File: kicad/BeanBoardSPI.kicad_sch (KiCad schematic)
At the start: 38 parts, among them J1 Power, J10 SPI6, J11 GPO, J12 GPO, J13 GPI, J14 GPI, J15 Power, J2 Address, J3 Data / Control, J4 SPI0 (RA8875), J5 SPI1, J6 SPI2, J7 SPI3, J8 SPI4, J9 SPI5, U1 74LS42, U10 74LS138, U2 74LS299, U3 74LS161, U4 74LS373, U5 74LS00, U6 74LS00, U7 74LS04, U8 74LS02, U9 74LS74

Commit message: Update BeanBoardSPI.kicad_sch
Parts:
- J1: footprint Connector_PinHeader_2.54mm:PinHeader_1x03_P2.54mm_Vertical -> AltFootprints:PinHeader_1x03_P2.54mm_Vertical
- J12, J13: footprint Connector_PinHeader_2.54mm:PinHeader_1x10_P2.54mm_Vertical -> AltFootprints:PinHeader_1x10_P2.54mm_Vertical
- J2, J3: footprint Connector_PinHeader_2.54mm:PinHeader_1x16_P2.54mm_Vertical -> AltFootprints:PinHeader_1x16_P2.54mm_Vertical
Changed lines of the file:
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@@
       (effects (font (size 1.27 1.27)))
     )
-    (property "Footprint" "Connector_PinHeader_2.54mm:PinHeader_1x03_P2.54mm_Vertical" (at 73.66 13.97 0)
+    (property "Footprint" "AltFootprints:PinHeader_1x03_P2.54mm_Vertical" (at 73.66 13.97 0)
       (effects (font (size 1.27 1.27)) hide)
     )
@@
       (effects (font (size 1.27 1.27)))
     )
-    (property "Footprint" "Connector_PinHeader_2.54mm:PinHeader_1x16_P2.54mm_Vertical" (at 55.88 31.75 0)
+    (property "Footprint" "AltFootprints:PinHeader_1x16_P2.54mm_Vertical" (at 55.88 31.75 0)
       (effects (font (size 1.27 1.27)) hide)
     )
@@
       (effects (font (size 1.27 1.27)))
     )
-    (property "Footprint" "Connector_PinHeader_2.54mm:PinHeader_1x10_P2.54mm_Vertical" (at 73.66 38.1 0)
+    (property "Footprint" "AltFootprints:PinHeader_1x10_P2.54mm_Vertical" (at 73.66 38.1 0)
       (effects (font (size 1.27 1.27)) hide)
     )
@@
       (effects (font (size 1.27 1.27)))
     )
-    (property "Footprint" "Connector_PinHeader_2.54mm:PinHeader_1x10_P2.54mm_Vertical" (at 88.9 38.1 0)
+    (property "Footprint" "AltFootprints:PinHeader_1x10_P2.54mm_Vertical" (at 88.9 38.1 0)
       (effects (font (size 1.27 1.27)) hide)
     )
@@
       (effects (font (size 1.27 1.27)))
     )
-    (property "Footprint" "Connector_PinHeader_2.54mm:PinHeader_1x16_P2.54mm_Vertical" (at 34.29 31.75 0)
-      (effects (font (size 1.27 1.27)) hide)
-    )
+    (property "Footprint" "AltFootprints:PinHeader_1x16_P2.54mm_Vertical" (at 34.29 31.75 0)
+      (effects (font (size 1.27 1.27)) hide)
+    )

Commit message: schematic
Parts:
- removed U1: 74LS42, Package_DIP:DIP-16_W7.62mm_Socket, symbol 74xx:74LS42
- removed U2: 74LS299, Package_DIP:DIP-20_W7.62mm_Socket, symbol 74xx:74LS299
- removed U3: 74LS161, Package_DIP:DIP-16_W7.62mm_Socket, symbol 74xx:74LS161
- removed U5, U6: 74LS00, Package_DIP:DIP-14_W7.62mm_Socket, symbol 74xx:74LS00
- removed unit 4 of U7
- removed unit 3 of U7
- removed unit 6 of U7
- removed unit 5 of U7
- removed unit 1 of U8
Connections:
- net CTRL_LATCH renamed CTRL_WR
- no-connect marks 47 -> 37
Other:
- note removed: "Counter / Decoder"
- note removed: "I/O Shift Register"
- moved on the sheet: J10, J4, J5, J6, J7, J8, J9, JP1, JP2, JP3, U10, U4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

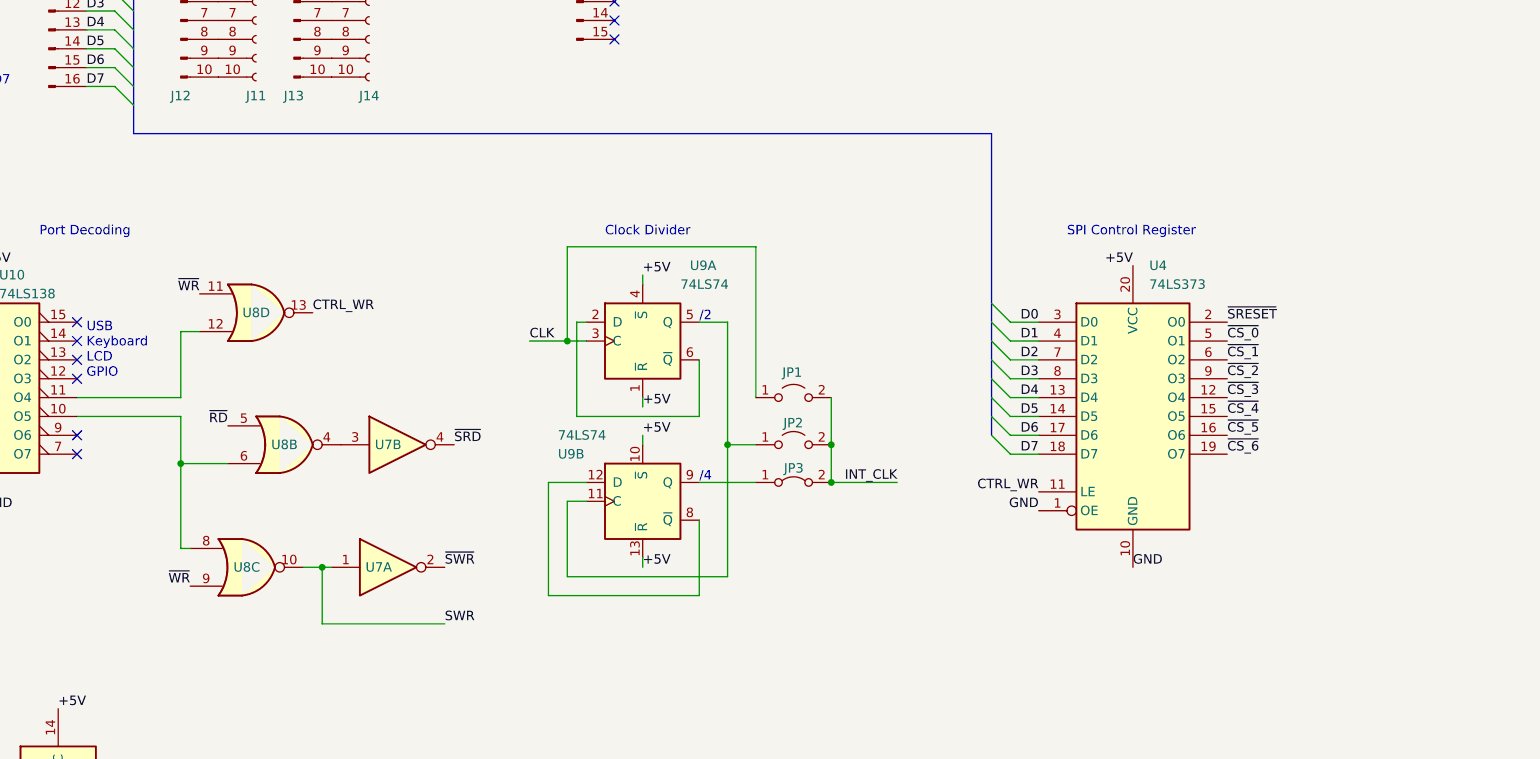
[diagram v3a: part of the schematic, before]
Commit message: align labels between simulation and schematic
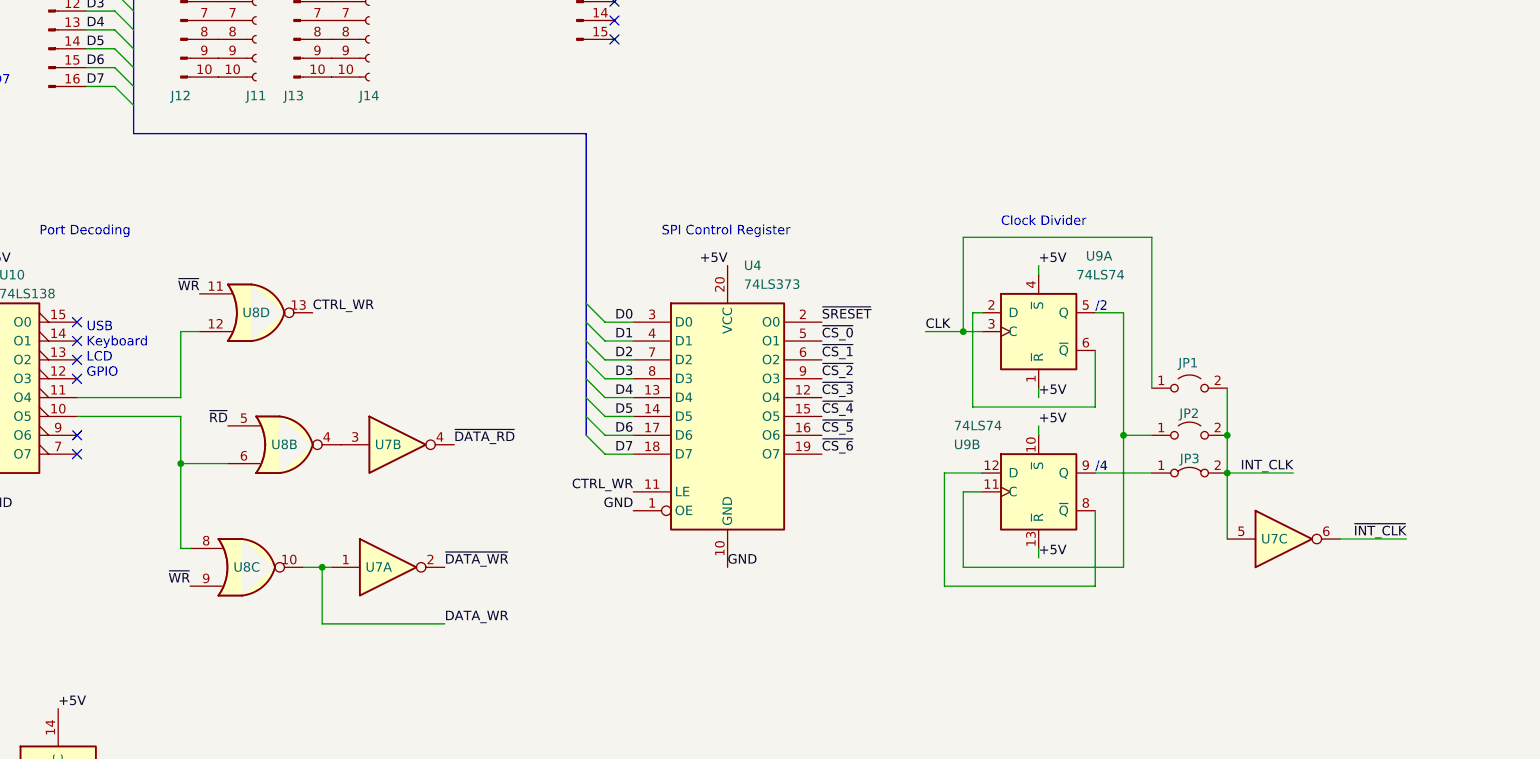
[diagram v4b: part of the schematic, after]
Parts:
- added unit 3 of U7
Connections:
- net INT_CLK: now also U7.5
- net SWR renamed DATA_WR
- net ~{SRD} renamed ~{DATA_RD}
- net ~{SWR} renamed ~{DATA_WR}
- new net ~{INT_CLK}: U7.6
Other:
- moved on the sheet: JP1, JP2, JP3, U4, U9A, U9B

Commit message: schematic
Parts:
- added U1: 74HC244, symbol 74xx:74HC244
- added U2: 74HC164, symbol 74xx:74HC164
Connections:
- net +5V: now also U1.20 (VCC), U2.14 (VCC)
- net D0: now also U1.18 (1Y0)
- net D1: now also U1.16 (1Y1)
- net D2: now also U1.14 (1Y2)
- net D3: now also U1.12 (1Y3)
- net D4: now also U1.3 (2Y0)
- net D5: now also U1.5 (2Y1)
- net D6: now also U1.7 (2Y2)
- net D7: now also U1.9 (2Y3)
- net GND: now also U1.10 (GND), U2.7 (GND)
- net SER_IN: now also U2.1 (DSA)
- net ~{DATA_RD}: now also U1.1 (1OE), U1.19 (2OE)
- net ~{DATA_WR}: now also U2.9 (~{MR})
- net SCLK renamed SER_CLK
- net SER_CLK: now also U2.8 (CP)
- new net: U1.11 (2A3), U2.13 (Q7)
- new net: U1.13 (2A2), U2.12 (Q6)
- new net: U1.15 (2A1), U2.11 (Q5)
- new net: U1.17 (2A0), U2.10 (Q4)
- new net: U1.2 (1A0), U2.3 (Q0)
- new net: U1.4 (1A1), U2.4 (Q1)
- new net: U1.6 (1A2), U2.5 (Q2)
- new net: U1.8 (1A3), U2.6 (Q3)
- new net SER_EN: U2.2 (DSB)
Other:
- moved on the sheet: JP1, JP2, JP3, U7C, U7G, U8E, U9A, U9B, U9C

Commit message: schematic
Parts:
- added U11, U3, U5, U6: 74HC165, symbol 74xx:74HC165
- added U12: 74HC08, symbol 74xx:74LS08
- added unit 4 of U7
- added unit 6 of U7
- added unit 5 of U7
- added unit 1 of U8
- U10: value 74LS138 -> 74HC138; symbol 74xx:74LS138 -> 74xx:74HC138
- U4: value 74LS373 -> 74HC373; symbol 74xx:74LS373 -> 74xx:74HC373
- U7: value 74LS04 -> 74HC04; symbol 74xx:74LS04 -> 74xx:74HC04
- U8: value 74LS02 -> 74HC02; symbol 74xx:74LS02 -> 74xx:74HC02
- U9: value 74LS74 -> 74HC74; symbol 74xx:74LS74 -> 74xx:74HC74
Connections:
- net +5V: now also U11.16 (VCC), U12.14 (VCC), U3.11 (D0), U3.12 (D1), U3.13 (D2), U3.14 (D3), U3.16 (VCC), U3.3 (D4), U3.4 (D5), U3.5 (D6), U5.16 (VCC), U6.16 (VCC), U6.6 (D7)
- net D0: now also U11.6 (D7)
- net D1: now also U5.11 (D0)
- net D2: now also U5.12 (D1)
- net D3: now also U5.13 (D2)
- net D4: now also U5.14 (D3)
- net D5: now also U5.3 (D4)
- net D6: now also U5.4 (D5)
- net D7: now also U5.5 (D6)
- net DATA_WR: now also U11.15 (~{CE}), U3.15 (~{CE}), U5.15 (~{CE}), U6.15 (~{CE})
- net GND: now also U11.10 (DS), U11.11 (D0), U11.12 (D1), U11.13 (D2), U11.14 (D3), U11.3 (D4), U11.4 (D5), U11.5 (D6), U11.8 (GND), U12.10, U12.12, U12.13, U12.4, U12.5, U12.7 (GND), U12.9, U3.6 (D7), U3.8 (GND), U5.6 (D7), U5.8 (GND), U6.10 (DS), U6.11 (D0), U6.12 (D1), U6.13 (D2), U6.14 (D3), U6.3 (D4), U6.4 (D5), U6.5 (D6), U6.8 (GND), U7.11, U7.13, U7.9, U8.2, U8.3
- net INT_CLK: now also U11.2 (CP), U3.2 (CP), U5.2 (CP), U6.2 (CP)
- net SER_CLK: now also U12.3
- net SER_EN: now also U12.1, U3.9 (Q7)
- net SER_OUT: now also U5.9 (Q7)
- net ~{DATA_WR}: now also U11.1 (~{PL}), U3.1 (~{PL}), U5.1 (~{PL}), U6.1 (~{PL})
- net ~{INT_CLK}: no longer names the net of U7.6
- net ~{INT_CLK}: now also U12.2
- new net: U11.9 (Q7), U5.10 (DS)
- new net: U3.10 (DS), U6.9 (Q7)
- no-connect marks 37 -> 48
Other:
- note added: "Counter-Decoder"
- note added: "Data Input Buffer"
- note added: "Serial In"
- note added: "Serial Out"
- moved on the sheet: JP1, JP2, JP3, U7C, U9A, U9B

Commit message: schematic
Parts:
- removed U12: 74HC08, symbol 74xx:74LS08
- JP3: value CLK/4 -> Jumper_2_Bridged
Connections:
- net GND: no longer U8.2, U8.3
- net INT_CLK: now also U8.3; no longer U7.5
- net SER_CLK: now also U8.1
- net SER_EN: now also U7.5
- net at U7.6: now also U8.2
- no-connect marks 48 -> 44
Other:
- moved on the sheet: U7C, U7D, U7E, U7F, U8A
